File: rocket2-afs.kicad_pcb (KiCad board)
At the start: 4 copper layers, 0 parts

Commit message: New MI-9653S-SMT-TR Buzzer and Buzzer Circuit. Added power footprint.
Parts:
- added BZ1: Buzzer, UCIRP-KiCAD-Lib:CUI_CMI-9653S-SMT, F.Cu at (127.4, 93.8)
- added C1: 100nF, Capacitor_SMD:C_0603_1608Metric, F.Cu at (30.5, 139.8)
- added C10: 10uF, Capacitor_SMD:C_0603_1608Metric, F.Cu at (34.5, 142.3)
- added C11: 100nF, Capacitor_SMD:C_0603_1608Metric, F.Cu at (34.5, 144.8)
- added C12: 100nF, Capacitor_SMD:C_0603_1608Metric, F.Cu at (34.5, 147.3)
- added C13: 100nF, Capacitor_SMD:C_0603_1608Metric, F.Cu at (34.5, 149.8)
- added C14: 100nF, Capacitor_SMD:C_0603_1608Metric, F.Cu at (34.5, 152.3)
- added C15: 100nF, Capacitor_SMD:C_0603_1608Metric, F.Cu at (34.5, 154.9)
- added C16: 100nF, Capacitor_SMD:C_0603_1608Metric, F.Cu at (34.5, 157.4)
- added C17: 100nF, Capacitor_SMD:C_0603_1608Metric, F.Cu at (38.5, 139.8)
- added C18: 100nF, Capacitor_SMD:C_0603_1608Metric, F.Cu at (38.5, 142.3)
- added C19: 100nF, Capacitor_SMD:C_0603_1608Metric, F.Cu at (38.5, 144.8)
- added C2: 100nF, Capacitor_SMD:C_0603_1608Metric, F.Cu at (30.5, 142.3)
- added C20: 100nF, Capacitor_SMD:C_0603_1608Metric, F.Cu at (38.5, 147.3)
- added C3: 100nF, Capacitor_SMD:C_0603_1608Metric, F.Cu at (30.5, 144.8)
- added C4: 100nF, Capacitor_SMD:C_0603_1608Metric, F.Cu at (30.5, 147.3)
- added C5: 100nF, Capacitor_SMD:C_0603_1608Metric, F.Cu at (30.5, 149.8)
- added C6: 100nF, Capacitor_SMD:C_0603_1608Metric, F.Cu at (30.5, 152.3)
- added C7: 100nF, Capacitor_SMD:C_0603_1608Metric, F.Cu at (30.5, 154.9)
- added C8: 100nF, Capacitor_SMD:C_0603_1608Metric, F.Cu at (30.5, 157.4)
- added C9: 10uF, Capacitor_SMD:C_0603_1608Metric, F.Cu at (34.5, 139.8)
- added D1: RED_LED, Diode_SMD:D_0603_1608Metric, F.Cu at (73.2, 154.3)
- added D2: GREEN_LED, Diode_SMD:D_0603_1608Metric, F.Cu at (73.2, 156.9)
- added D3: BLUE_LED, Diode_SMD:D_0603_1608Metric, F.Cu at (73.2, 159.5)
- added D4: YELLOW_LED, Diode_SMD:D_0603_1608Metric, F.Cu at (73.2, 162.1)
- added J1: ARMING_PLUG, TerminalBlock:TerminalBlock_bornier-2_P5.08mm, F.Cu at (174.4, 106.0)
- added J2: POWER, TerminalBlock:TerminalBlock_bornier-2_P5.08mm, F.Cu at (186.0, 91.7)
- added J3: E-MATCH_DROGUE, TerminalBlock:TerminalBlock_bornier-2_P5.08mm, F.Cu at (140.7, 106.0)
- added J4: SWD, Connector_PinHeader_1.27mm:PinHeader_2x05_P1.27mm_Vertical_SMD, F.Cu at (158.6, 72.8)
- added J5: E-MATCH_RECOVERY, TerminalBlock:TerminalBlock_bornier-2_P5.08mm, F.Cu at (157.4, 106.0)
- added J6: ~, Connector_USB:USB_C_Receptacle_GCT_USB4105-xx-A_16P_TopMnt_Horizontal, F.Cu at (186.3, 76.5)
- added Q1: Q_NMOS_GSD, Package_TO_SOT_SMD:TSOT-23, F.Cu at (31.1, 160.8)
- added Q2: Q_NMOS_GSD, Package_TO_SOT_SMD:TSOT-23, F.Cu at (31.1, 165.3)
- added Q3: Q_NMOS_GSD, Package_TO_SOT_SMD:TSOT-23, F.Cu at (31.1, 169.8)
- added Q4: Q_NMOS_GSD, Package_TO_SOT_SMD:TSOT-23, F.Cu at (31.1, 174.2)
- added Q5: Q_NMOS_GSD, Package_TO_SOT_SMD:TSOT-23, F.Cu at (31.1, 178.7)
- added R1: 1k, Resistor_SMD:R_0603_1608Metric, F.Cu at (38.5, 149.8)
- added R10: 470, Resistor_SMD:R_0603_1608Metric, F.Cu at (42.5, 152.3)
- added R11: 1k, Resistor_SMD:R_0603_1608Metric, F.Cu at (42.5, 154.9)
- added R12: 1k, Resistor_SMD:R_0603_1608Metric, F.Cu at (42.5, 157.4)
- added R13: 4k7, Resistor_SMD:R_0603_1608Metric, F.Cu at (46.5, 139.8)
- added R14: 4k7, Resistor_SMD:R_0603_1608Metric, F.Cu at (46.5, 142.3)
- added R15: 5k1, Resistor_SMD:R_0603_1608Metric, F.Cu at (46.5, 144.8)
- added R16: 5k1, Resistor_SMD:R_0603_1608Metric, F.Cu at (46.5, 147.3)
- added R17: 4k7, Resistor_SMD:R_0603_1608Metric, F.Cu at (46.5, 149.8)
- added R18: 4k7, Resistor_SMD:R_0603_1608Metric, F.Cu at (46.5, 152.3)
- added R19: 1k, Resistor_SMD:R_0603_1608Metric, F.Cu at (46.5, 154.9)
- added R2: 3k3, Resistor_SMD:R_0603_1608Metric, F.Cu at (38.5, 152.3)
- added R3: 1k, Resistor_SMD:R_0603_1608Metric, F.Cu at (38.5, 154.9)
- added R4: 1k, Resistor_SMD:R_0603_1608Metric, F.Cu at (38.5, 157.4)
- added R5: 1k, Resistor_SMD:R_0603_1608Metric, F.Cu at (42.5, 139.8)
- added R6: 470, Resistor_SMD:R_0603_1608Metric, F.Cu at (42.5, 142.3)
- added R7: 470, Resistor_SMD:R_0603_1608Metric, F.Cu at (42.5, 144.8)
- added R8: 1k, Resistor_SMD:R_0603_1608Metric, F.Cu at (42.5, 147.3)
- added R9: 470, Resistor_SMD:R_0603_1608Metric, F.Cu at (42.5, 149.8)
- added U1: ~, Package_QFP:LQFP-64_10x10mm_P0.5mm, F.Cu at (155.2, 85.2)
- added U2: LD1086DT33TR, Package_TO_SOT_SMD:TO-252-2, F.Cu at (172.6, 96.1)
- added U3: ~, RF_GPS:ublox_SAM-M8Q, F.Cu at (144.5, 69.1)
- added U4: ~, Package_SO:SOIC-8W_5.3x5.3mm_P1.27mm, F.Cu at (170.2, 87.0)
- added U5: ~, UCIRP-KiCAD-Lib:BMI088, F.Cu at (165.4, 77.6)
- added U6: ~, UCIRP-KiCAD-Lib:MS5607-02BA, F.Cu at (153.0, 94.9)
- added U7: ~, Package_CSP:WLCSP-12_1.56x1.56mm_P0.4mm, F.Cu at (157.6, 96.0)
- added U8: USBLC6-2SC6, Package_TO_SOT_SMD:SOT-23-6, F.Cu at (178.0, 77.2)
- added Y1: 16MHz, Crystal:Crystal_SMD_2520-4Pin_2.5x2.0mm, F.Cu at (145.5, 83.7)
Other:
- board outline added: 70 x 50 mm

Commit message: Complete PCB, first iteration
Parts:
- BZ1: footprint UCIRP-KiCAD-Lib:CUI_CMI-9653S-SMT -> Buzzer_Beeper:Buzzer_CUI_CPT-9019S-SMT
- moved C15 168.3 mm to (185.8, 81.2), turned to -90 degrees
- moved C13 165.7 mm to (179.5, 69.7)
- moved C14 164.0 mm to (176.1, 69.7), turned to 180 degrees
- moved R10 155.2 mm to (171.9, 66.7), turned to 90 degrees
- moved R7 154.6 mm to (175.8, 66.7), turned to 90 degrees
- moved C7 154.4 mm to (162.6, 74.8), turned to -90 degrees
- moved C6 153.0 mm to (158.2, 68.2)
- moved C9 152.7 mm to (178.7, 89.5)
- moved C10 150.6 mm to (175.5, 89.5), turned to 180 degrees
- moved R9 150.5 mm to (167.9, 66.7), turned to 90 degrees
- moved C5 150.3 mm to (163.3, 79.5)
- moved Q5 146.0 mm to (145.8, 88.2), turned to 180 degrees
- moved Q4 145.8 mm to (156.0, 98.9), turned to 90 degrees
- moved C3 143.3 mm to (159.8, 83.0), turned to -90 degrees
- moved R6 143.1 mm to (164.0, 66.7), turned to 90 degrees
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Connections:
- J6 pad A6: USB_DP_CON -> USB_CONN_D+
- J6 pad A7: USB_DM_CON -> USB_CONN_D-
- J6 pad B6: USB_DP_CON -> USB_CONN_D+
- J6 pad B7: USB_DM_CON -> USB_CONN_D-
- U1 pad 14: BUZZER_PWM -> unconnected-(U1-PA0-Pad14)
- U1 pad 44: USB_DM -> USB_D-
- U1 pad 45: USB_DP -> USB_D+
- U1 pad 55: unconnected-(U1-PB3-Pad55) -> BUZZER_PWM
- U8 pad 1: USB_DM -> USB_CONN_D-
- U8 pad 3: USB_DP -> USB_CONN_D+
- U8 pad 4: USB_DP_CON -> USB_D+
- U8 pad 6: USB_DM_CON -> USB_D-
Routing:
- net +3.3V: track 0.00 -> 58.6 mm, vias 0 -> 55
- net NRST: track 0.00 -> 47.9 mm, vias 0 -> 2
- net DROGUE: track 0.00 -> 45.5 mm, vias 0 -> 2
- net RECOVERY_CONT: track 0.00 -> 40.6 mm, vias 0 -> 2
- net DROGUE_CONT: track 0.00 -> 40.6 mm, vias 0 -> 2
- net RECOVERY: track 0.00 -> 37.3 mm, vias 0 -> 2
- net ARM_CONT: track 0.00 -> 34.1 mm, vias 0 -> 2
- net VCC: track 0.00 -> 33.0 mm
- net VBUS: track 0.00 -> 32.9 mm
- net GPS_INT: track 0.00 -> 30.8 mm, vias 0 -> 2
- net GPS_RESET: track 0.00 -> 29.4 mm, vias 0 -> 2
- net DEBUCK_SWCLK: track 0.00 -> 28.0 mm
- net GPS_SCL: track 0.00 -> 26.5 mm
- net DEBUG_SWDIO: track 0.00 -> 26.4 mm
- net MEM_MISO: track 0.00 -> 25.8 mm
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- added copper zone on In2.Cu, net +3.3V
- added copper zone on In2.Cu, net ARM_POWER
- added copper zone on B.Cu, net GND
- added copper zone on F.Cu, net GND
- added copper zone on In1.Cu, net GND
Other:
- board text added: "AFS 2.1 {dblquote}Betelgeuse{dblquote} 2/21/2024 Caden Nguyen Robert Woo"
- board text added: "ALTIMETER"
- board text added: "ARMED"
- board text added: "ARMING PLUG"
- board text added: "BUZZER"
- board text added: "DEBUG"
- board text added: "DROGUE"
- board text added: "FLIGHT"
- board text added: "GPS"
- board text added: "HSE"
- board text added: "IMU"
- board text added: "LDO"
- board text added: "MAG"
- board text added: "MAIN"
- board text added: "MCU"
- board text added: "MEMORY"
- board text added: "POWER"
- board text added: "STANDBY"
- board text added: "STORAGE"
- board text added: "USB-C"

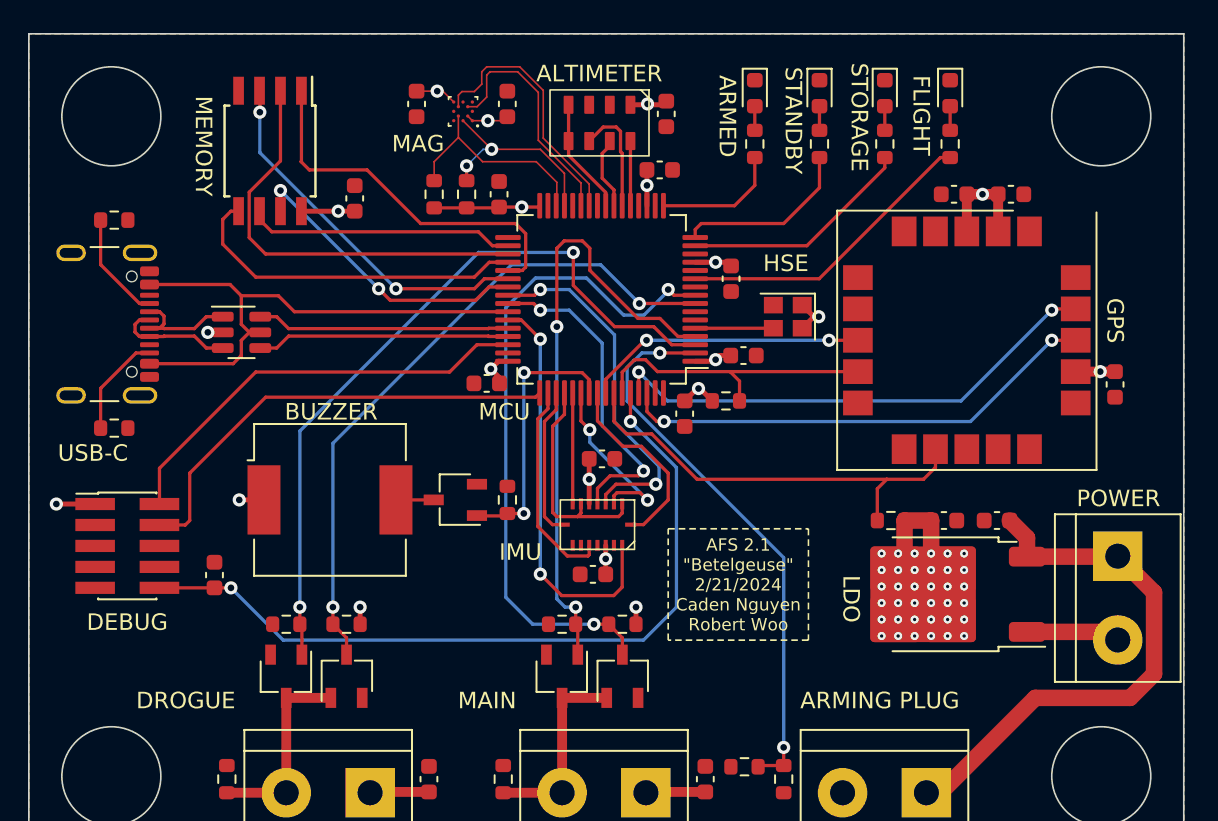
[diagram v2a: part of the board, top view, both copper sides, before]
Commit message: Current limiting resistors to MOSFETs. Silkscreen names + Logo. Adjusted BMI088 footprint as per ERC error (LOCAL TO PCB).
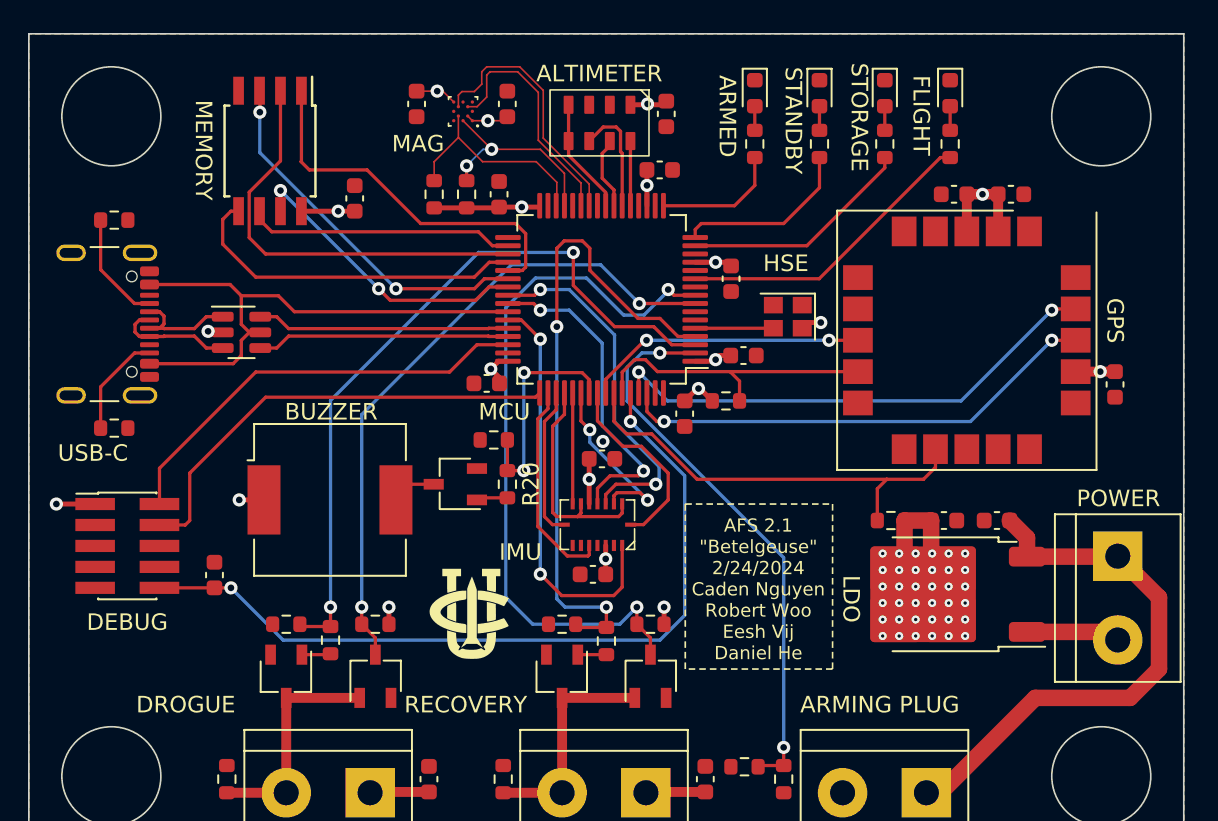
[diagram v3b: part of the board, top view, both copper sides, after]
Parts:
- added R20: 100, Resistor_SMD:R_0603_1608Metric, F.Cu at (149.0, 87.3)
- added R21: 100, Resistor_SMD:R_0603_1608Metric, F.Cu at (138.3, 96.8)
- added R22: 100, Resistor_SMD:R_0603_1608Metric, F.Cu at (155.0, 96.8)
- R19: value 1k -> 10k
- R5, R8: value 1k -> 100k
- moved R19 3.73 mm to (148.2, 84.6), turned to 180 degrees
- moved Q1 1.75 mm to (141.0, 98.9)
- moved R3 1.75 mm to (141.0, 95.8)
- moved Q4 1.70 mm to (157.7, 98.9)
- moved R12 1.70 mm to (157.7, 95.8)
- moved Q5 0.95 mm to (145.8, 87.3)
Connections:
- Q2 pad 1: DROGUE -> Net-(Q2-G)
- Q3 pad 1: RECOVERY -> Net-(Q3-G)
- Q5 pad 1: BUZZER_PWM -> Net-(Q5-G)
- R19 pad 1: BUZZER_PWM -> BUZZER
- U1 pad 55: BUZZER_PWM -> BUZZER
- Y1 pad 1: +3.3V -> unconnected-(Y1-Pad1)
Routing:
- net BUZZER_PWM: track 16.2 -> 0.00 mm, vias 2 -> 0
- net BUZZER: track 0.00 -> 13.7 mm, vias 0 -> 2
- net RECOVERY_CONT: track 40.6 -> 43.8 mm
- net RECOVERY: track 37.3 -> 39.4 mm
- net Net-(Q5-G): track 0.00 -> 1.90 mm
- net Net-(Q2-G): track 0.00 -> 1.76 mm
- net Net-(J3-Pin_2): track 12.1 -> 13.8 mm
- net Net-(Q3-G): track 0.00 -> 1.73 mm
- net Net-(J5-Pin_2): track 12.0 -> 13.7 mm
- net NRST: track 47.9 -> 48.6 mm
- net DROGUE_CONT: track 40.6 -> 39.8 mm
- net +3.3V: track 58.6 -> 58.1 mm
- net GND: track 6.74 -> 6.75 mm, vias 1 -> 2
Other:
- board text added: "AFS 2.1 {dblquote}Betelgeuse{dblquote} 2/24/2024 Caden Nguyen Robert Woo Eesh Vij Daniel He"
- board text added: "RECOVERY"
- board text removed: "AFS 2.1 {dblquote}Betelgeuse{dblquote} 2/21/2024 Caden Nguyen Robert Woo"
- board text removed: "MAIN"
